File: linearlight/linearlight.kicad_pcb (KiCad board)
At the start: 2 copper layers, 136.7 x 59.7 mm, 72 parts, among them J1 Screw_Terminal, J2 Conn_01x04_Pin, J3 Conn_01x19_Socket, J4 Conn_01x19_Socket, J5 Conn_01x04_Pin, Q1 FQP30N06, Q2 FQP30N06, Q3 FQP30N06, Q4 FQP30N06, Q5 2N3904, Q6 2N3904, Q7 2N3904, Q8 2N3904, U1 TLV5620CN, U2 ESP32 DevKitC, U3 MC33204, U4 LM4040LP-2.5

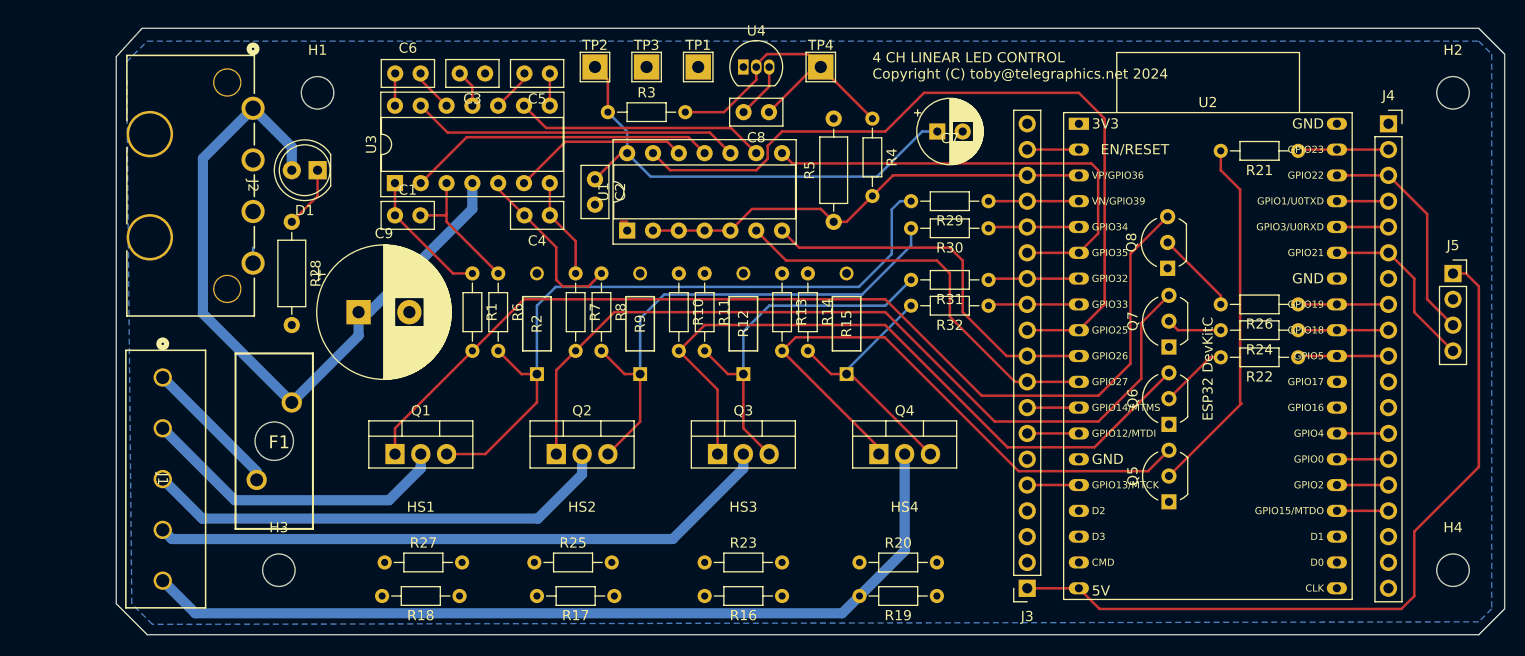
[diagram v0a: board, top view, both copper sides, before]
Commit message: Updates including 2nd DAC for nonlinear response.
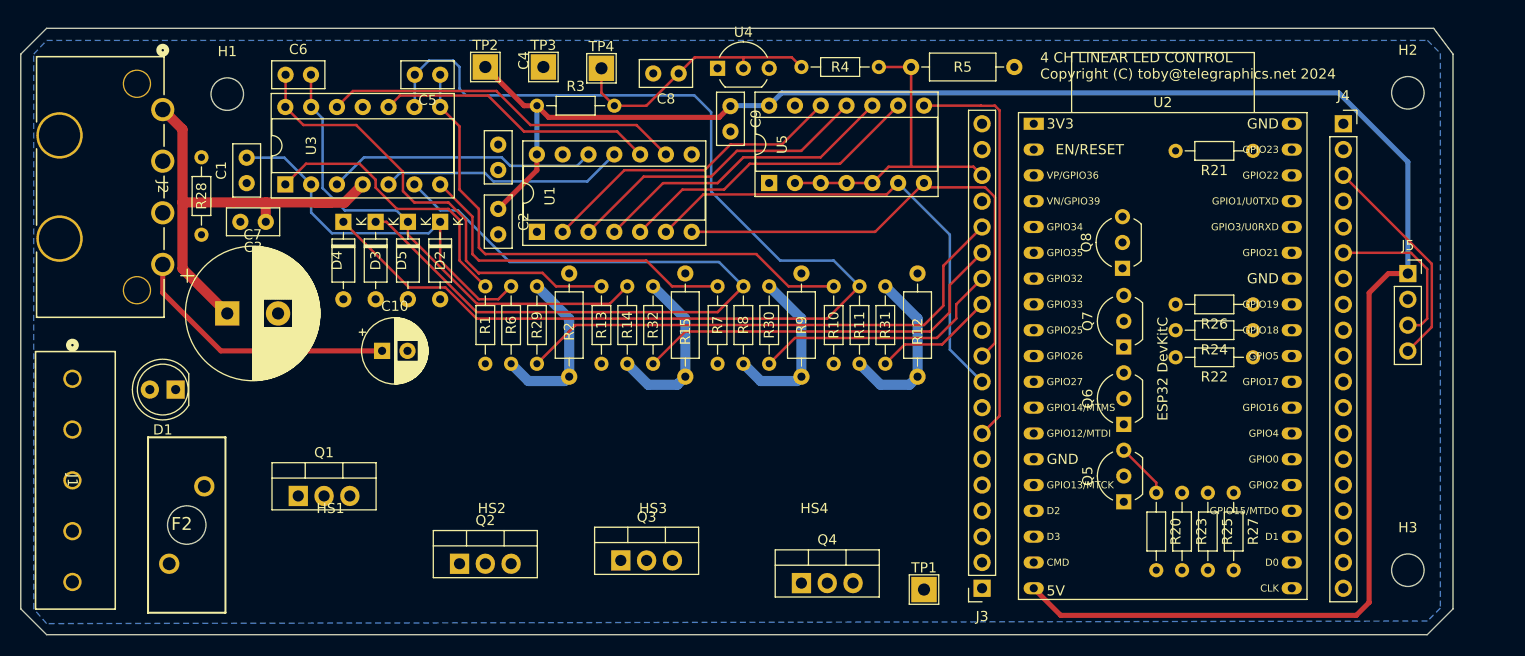
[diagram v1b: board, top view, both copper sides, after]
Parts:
- removed F1: Fuse, Fuse:01530008
- removed H4: MountingHole, MountingHole:MountingHole_3.2mm_M3
- removed R16, R17, R18, R19: 100k, Resistor_THT:R_Axial_DIN0204_L3.6mm_D1.6mm_P7.62mm_Horizontal
- added C10: 100u, Capacitor_THT:CP_Radial_D6.3mm_P2.50mm, F.Cu at (161.3, 116.8)
- added D2: 1N4148, Diode_THT:D_DO-35_SOD27_P7.62mm_Horizontal, F.Cu at (167.0, 104.1)
- added D3: 1N4148, Diode_THT:D_DO-35_SOD27_P7.62mm_Horizontal, F.Cu at (160.7, 104.1)
- added D4: 1N4148, Diode_THT:D_DO-35_SOD27_P7.62mm_Horizontal, F.Cu at (157.5, 104.1)
- added D5: 1N4148, Diode_THT:D_DO-35_SOD27_P7.62mm_Horizontal, F.Cu at (163.8, 104.1)
- added F2: Fuse, Fuse:01530008, F.Cu at (142.1, 134.0)
- added U5: TLV5620CN, Package_DIP:DIP-14_W7.62mm_Socket, F.Cu at (199.4, 100.3)
- C7: value 100u -> 2200uF; footprint Capacitor_THT:CP_Radial_D6.3mm_P2.50mm -> Capacitor_THT:CP_Radial_D13.0mm_P5.00mm
- C9: value 2200uF -> 1u; footprint Capacitor_THT:CP_Radial_D13.0mm_P5.00mm -> Capacitor_THT:C_Disc_D5.0mm_W2.5mm_P2.50mm
- H1, H2, H3: value MountingHole -> ~
- HS1, HS2, HS3, HS4: value Heatsink -> ~
- R12, R15, R2, R9: footprint Resistor_THT:RES_WLAR100FET -> Resistor_THT:R_Axial_DIN0207_L6.3mm_D2.5mm_P10.16mm_Horizontal
- R28: footprint Resistor_THT:R_Axial_DIN0207_L6.3mm_D2.5mm_P10.16mm_Horizontal -> Resistor_THT:R_Axial_DIN0204_L3.6mm_D1.6mm_P7.62mm_Horizontal
- R4: value 4.7k -> 10k
- U4: footprint Package_TO_SOT_THT:TO-92_Inline -> Package_TO_SOT_THT:TO-92_Inline_Wide
- moved H3 111.1 mm to (262.3, 138.4)
- moved R27 83.8 mm to (245.1, 130.8), turned to -90 degrees
- moved C7 72.1 mm to (146.1, 113.2)
- moved R25 66.6 mm to (242.6, 130.8), turned to -90 degrees
- moved TP1 56.0 mm to (214.6, 140.3)
- moved R23 47.5 mm to (240.0, 130.8), turned to -90 degrees
- moved R29 47.2 mm to (176.5, 118.1), turned to 90 degrees
- moved C9 41.8 mm to (195.6, 92.8), turned to -90 degrees
- moved R32 33.5 mm to (188.0, 118.1), turned to 90 degrees
- moved R20 30.0 mm to (237.5, 130.8), turned to -90 degrees
- moved C3 26.1 mm to (149.8, 104.1)
- moved D1 25.7 mm to (141.0, 120.7)
- moved R30 25.4 mm to (199.4, 118.1), turned to 90 degrees
- moved TP4 21.6 mm to (182.9, 89.0)
- moved R13 17.8 mm to (182.9, 110.5)
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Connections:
- C1 pad 2: Net-(U3A-IN+) -> Net-(D2-K)
- C4 pad 2: Net-(U3B-IN+) -> Net-(D3-K)
- C5 pad 2: Net-(U3C-IN+) -> Net-(D4-K)
- C6 pad 2: Net-(U3D-IN+) -> Net-(D5-K)
- C7 pad 1: +5V -> +12V
- C9 pad 1: +12V -> +5V
- J5 pad 3: Net-(J4-Pin_3) -> Net-(J4-Pin_6)
- J5 pad 4: Net-(J4-Pin_6) -> Net-(J4-Pin_3)
- R11 pad 1: Net-(U3C-IN+) -> Net-(D4-K)
- R14 pad 1: Net-(U3D-IN+) -> Net-(D5-K)
- R29 pad 1: Net-(J3-Pin_16) -> Net-(J3-Pin_15)
- R30 pad 1: Net-(J3-Pin_15) -> Net-(J3-Pin_13)
- R31 pad 1: Net-(J3-Pin_13) -> Net-(J3-Pin_12)
- R32 pad 1: Net-(J3-Pin_12) -> Net-(J3-Pin_14)
- R6 pad 1: Net-(U3A-IN+) -> Net-(D2-K)
- R8 pad 1: Net-(U3B-IN+) -> Net-(D3-K)
- U1 pad 2: Net-(J3-Pin_17) -> Net-(U1-REFA)
- U1 pad 3: Net-(J3-Pin_17) -> Net-(U1-REFB)
- U1 pad 4: Net-(J3-Pin_17) -> Net-(U1-REFC)
- U1 pad 5: Net-(J3-Pin_17) -> Net-(U1-REFD)
- U3 pad 10: Net-(U3C-IN+) -> Net-(U1-DACC)
- U3 pad 12: Net-(U3D-IN+) -> Net-(U1-DACD)
- U3 pad 13: Net-(U1-DACC) -> Net-(D5-K)
- U3 pad 2: Net-(U1-DACB) -> Net-(D2-K)
- U3 pad 3: Net-(U3A-IN+) -> Net-(U1-DACA)
- U3 pad 5: Net-(U3B-IN+) -> Net-(U1-DACB)
- U3 pad 6: Net-(U1-DACA) -> Net-(D3-K)
- U3 pad 9: Net-(U1-DACD) -> Net-(D4-K)
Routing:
- net Net-(D4-K): track 0.00 -> 118.6 mm
- net Net-(Q1-G): track 101.4 -> 0.00 mm
- net +5V: track 124.5 -> 215.9 mm
- net Net-(J1-Pin_5): track 86.4 -> 0.00 mm
- net Net-(Q2-G): track 83.7 -> 0.00 mm
- net Net-(D3-K): track 0.00 -> 77.5 mm
- net Net-(J3-Pin_11): track 77.1 -> 0.00 mm
- net Net-(Q3-G): track 69.1 -> 0.00 mm
- net Net-(J1-Pin_4): track 61.8 -> 0.00 mm
- net Net-(Q4-G): track 59.0 -> 5.51 mm
- net Net-(Q1-S): track 68.9 -> 16.8 mm
- net Net-(U3C-OUT): track 3.18 -> 55.1 mm
- net Net-(D5-K): track 0.00 -> 47.8 mm
- net Net-(J1-Pin_3): track 46.7 -> 0.00 mm
- net Net-(J3-Pin_15): track 8.89 -> 51.7 mm
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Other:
- board size 136.7 x 59.7 mm -> 141 x 59.7 mm

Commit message: PCB layout passes DRC.
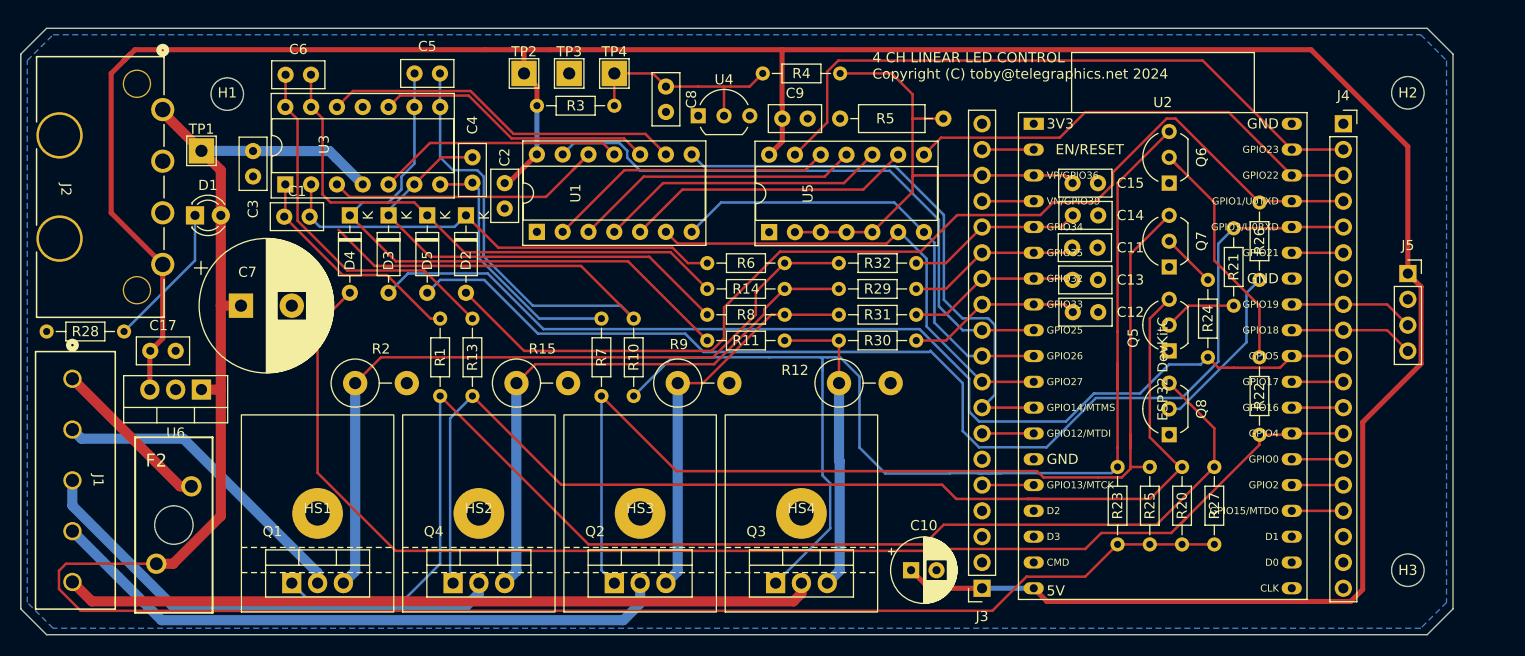
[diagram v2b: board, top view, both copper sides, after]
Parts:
- added C11: 0.1u, Capacitor_THT:C_Disc_D5.0mm_W2.5mm_P2.50mm, F.Cu at (231.7, 106.7)
- added C12: 0.1u, Capacitor_THT:C_Disc_D5.0mm_W2.5mm_P2.50mm, F.Cu at (231.8, 113.0)
- added C13: 0.1u, Capacitor_THT:C_Disc_D5.0mm_W2.5mm_P2.50mm, F.Cu at (231.8, 109.9)
- added C14: 0.1u, Capacitor_THT:C_Disc_D5.0mm_W2.5mm_P2.50mm, F.Cu at (231.8, 103.5)
- added C15: 0.1u, Capacitor_THT:C_Disc_D5.0mm_W2.5mm_P2.50mm, F.Cu at (231.8, 100.3)
- added C17: .1u, Capacitor_THT:C_Disc_D5.0mm_W2.5mm_P2.50mm, F.Cu at (138.5, 116.8)
- added U6: L7805, Package_TO_SOT_THT:TO-220-3_Vertical, F.Cu at (143.5, 120.7)
- D1: footprint LED_THT:LED_D5.0mm -> LED_THT:LED_D3.0mm
- HS1, HS2, HS3, HS4: footprint Heatsink:Max48 heatsink -> Heatsink:Max47 heatsink
- R12, R15, R2, R9: value 0.15 -> 0.5; footprint Resistor_THT:R_Axial_DIN0207_L6.3mm_D2.5mm_P10.16mm_Horizontal -> Resistor_THT:R_Axial_DIN0414_L11.9mm_D4.5mm_P5.08mm_Vertical
- R4: value 10k -> 2.2k
- moved TP1 83.2 mm to (143.5, 97.2)
- moved C10 56.4 mm to (213.4, 138.4)
- moved R29 38.1 mm to (213.9, 110.7), turned to 180 degrees
- moved Q4 34.3 mm to (168.3, 139.7)
- moved R32 27.7 mm to (213.9, 108.2), turned to 180 degrees
- moved Q6 24.2 mm to (238.8, 100.3)
- moved R2 21.1 mm to (158.6, 120.0), turned to 0 degrees
- moved R10 19.9 mm to (186.1, 113.7)
- moved R6 19.4 mm to (193.3, 108.2), turned to 0 degrees
- moved D1 17.3 mm to (142.9, 103.5), turned to 0 degrees
- moved Q8 17.0 mm to (238.8, 125.1)
- moved R15 16.6 mm to (174.5, 120.0), turned to 0 degrees
- moved R11 15.9 mm to (193.3, 115.8), turned to 0 degrees
- moved Q5 15.5 mm to (238.8, 116.8)
- moved Q3 15.4 mm to (200.0, 139.7)
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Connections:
- J4 pad 10: Net-(J4-Pin_10) -> Net-(D3-A)
- J4 pad 13: Net-(D2-A) -> Net-(D4-A)
- J4 pad 14: Net-(D3-A) -> Net-(J4-Pin_14)
- J4 pad 15: Net-(D4-A) -> Net-(J4-Pin_15)
- J4 pad 16: Net-(D5-A) -> Net-(J4-Pin_16)
- J4 pad 4: Net-(J4-Pin_4) -> Net-(D2-A)
- J4 pad 5: Net-(J4-Pin_5) -> Net-(D5-A)
- J5 pad 3: Net-(J4-Pin_6) -> Net-(J4-Pin_8)
- J5 pad 4: Net-(J4-Pin_3) -> Net-(J4-Pin_9)
- Q2 pad 2: Net-(J1-Pin_3) -> Net-(J1-Pin_4)
- Q3 pad 2: Net-(J1-Pin_4) -> Net-(J1-Pin_5)
- Q4 pad 2: Net-(J1-Pin_5) -> Net-(J1-Pin_3)
- R21 pad 1: Net-(J4-Pin_2) -> Net-(D5-A)
- R22 pad 1: Net-(J4-Pin_10) -> Net-(D4-A)
- R24 pad 1: Net-(J4-Pin_9) -> Net-(D3-A)
- R26 pad 1: Net-(J4-Pin_8) -> Net-(D2-A)
- R29 pad 1: Net-(J3-Pin_15) -> Net-(J3-Pin_14)
- R29 pad 2: Net-(Q1-S) -> Net-(Q4-S)
- R30 pad 1: Net-(J3-Pin_13) -> Net-(J3-Pin_12)
- R30 pad 2: Net-(Q2-S) -> Net-(Q3-S)
- R31 pad 1: Net-(J3-Pin_12) -> Net-(J3-Pin_13)
- R31 pad 2: Net-(Q3-S) -> Net-(Q2-S)
- R32 pad 1: Net-(J3-Pin_14) -> Net-(J3-Pin_15)
- R32 pad 2: Net-(Q4-S) -> Net-(Q1-S)
- U2 pad 23: Net-(D5-A) -> Net-(J4-Pin_16)
- U2 pad 24: Net-(D4-A) -> Net-(J4-Pin_15)
- U2 pad 25: Net-(D3-A) -> Net-(J4-Pin_14)
- U2 pad 26: Net-(D2-A) -> Net-(D4-A)
- U2 pad 29: Net-(J4-Pin_10) -> Net-(D3-A)
- U2 pad 34: Net-(J4-Pin_5) -> Net-(D5-A)
- U2 pad 35: Net-(J4-Pin_4) -> Net-(D2-A)
- U5 pad 13: unconnected-(U5-LDAC-Pad13) -> Net-(J4-Pin_2)
- U5 pad 8: Net-(J3-Pin_7) -> Net-(J4-Pin_3)
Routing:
- net +12V: track 44.6 -> 200.8 mm
- net Net-(D4-A): track 0.00 -> 129.6 mm
- net Net-(Q1-G): track 0.00 -> 128.6 mm
- net Net-(Q3-G): track 0.00 -> 125.3 mm
- net Net-(D5-A): track 0.00 -> 116.3 mm
- net Net-(Q4-G): track 5.51 -> 114.7 mm
- net Net-(D3-A): track 0.00 -> 106.2 mm
- net Net-(Q2-G): track 0.00 -> 104.4 mm
- net Net-(D2-A): track 0.00 -> 104.2 mm
- net Net-(J1-Pin_5): track 0.00 -> 73.9 mm
- net +5V: track 215.9 -> 286.3 mm
- net Net-(J4-Pin_2): track 0.00 -> 64.4 mm
- net Net-(J1-Pin_4): track 0.00 -> 62.2 mm
- net Net-(D4-K): track 118.6 -> 58.4 mm
- net Net-(J3-Pin_11): track 0.00 -> 59.9 mm
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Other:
- outline, holes or cut-outs redrawn

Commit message: Release candidate 1
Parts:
- added TP_VDAC1: VDAC, TestPoint:TestPoint_THTPad_2.5x2.5mm_Drill1.2mm, F.Cu at (216.4, 90.4)
- moved J5 2.05 mm to (262.1, 107.2)
- renumbered TP1 to TP+12, TP4 to TP+2.5, TP2 to TP+5, TP3 to TP_GND1
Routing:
- net Net-(J3-Pin_17): track 50.0 -> 56.7 mm
- net Net-(J4-Pin_8): track 12.3 -> 11.3 mm
- net Net-(J4-Pin_9): track 12.3 -> 11.3 mm
- net +5V: track 286.3 -> 287.3 mm
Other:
- board text added: "+ G R B W"
- board text added: "4 CHANNEL LINEAR LED CONTROL Copyright (C) toby@telegraphics.net 2024"
- board text added: "emilite 1.0"
- board text removed: "4 CH LINEAR LED CONTROL Copyright (C) toby@telegraphics.net 2024"

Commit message: Release candidate 2
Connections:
- U1 pad 13: Net-(J3-Pin_11) -> Net-(J3-Pin_10)
- U1 pad 6: Net-(J3-Pin_9) -> Net-(J3-Pin_8)
- U1 pad 7: Net-(J3-Pin_10) -> Net-(J3-Pin_9)
- U1 pad 8: Net-(J3-Pin_8) -> Net-(J3-Pin_11)
- U5 pad 6: Net-(J3-Pin_9) -> Net-(J3-Pin_8)
- U5 pad 7: Net-(J3-Pin_10) -> Net-(J3-Pin_9)
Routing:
- net Net-(Q3-G): track 125.3 -> 102.4 mm, vias 0 -> 1
- net Net-(J3-Pin_10): track 45.7 -> 60.7 mm
- net Net-(J3-Pin_11): track 59.9 -> 45.3 mm
- net Net-(J3-Pin_8): track 55.4 -> 49.8 mm
- net Net-(D5-A): track 116.3 -> 114.4 mm
- net Net-(D3-A): track 106.2 -> 104.3 mm
- net Net-(J3-Pin_9): track 47.1 -> 46.0 mm

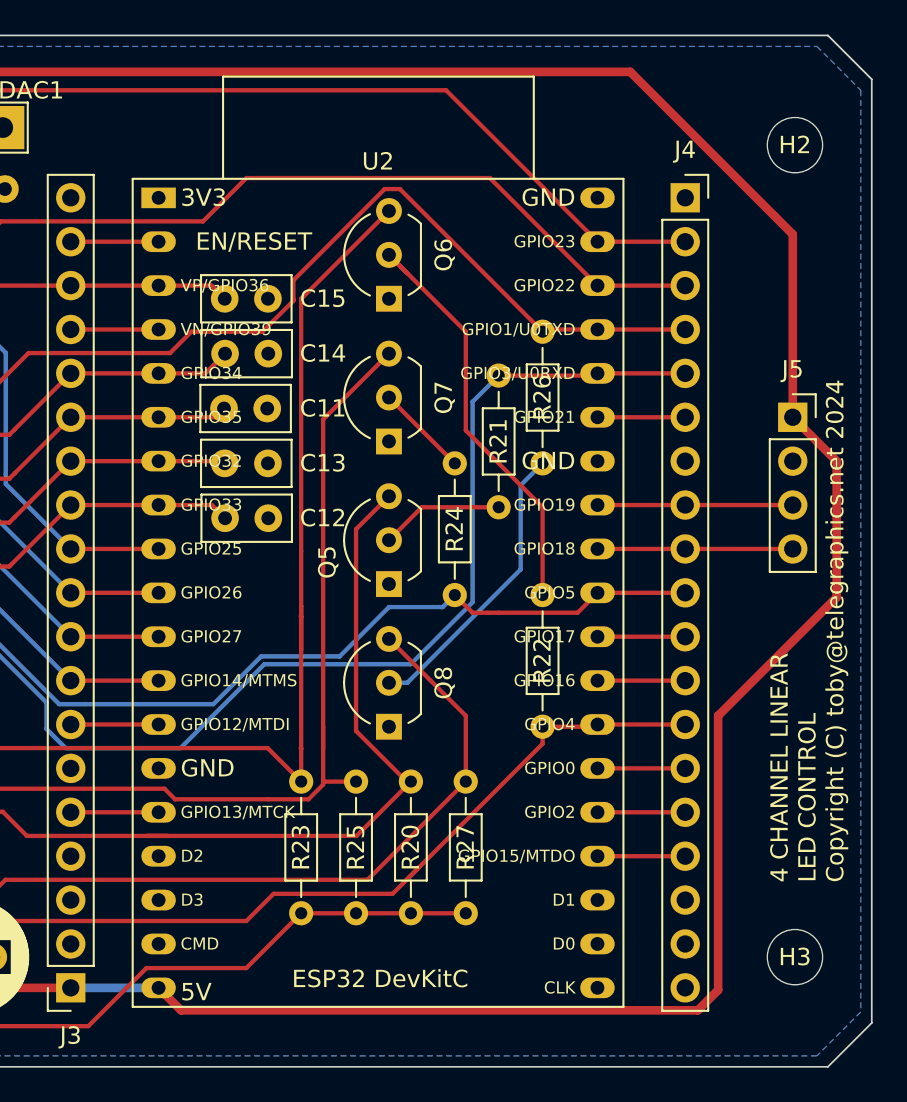
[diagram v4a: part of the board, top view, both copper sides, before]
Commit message: Add cnx for spectrometer.
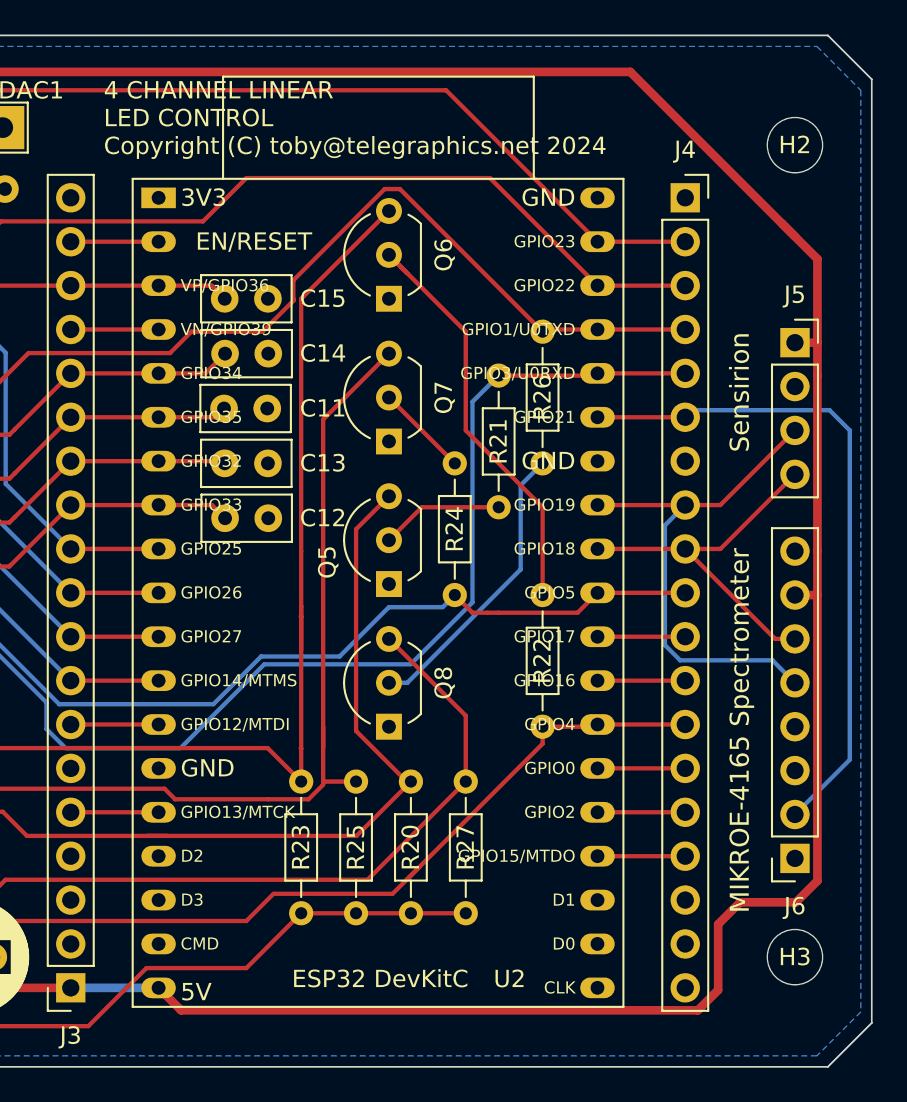
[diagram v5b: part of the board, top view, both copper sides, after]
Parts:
- added J6: Conn_01x08_Socket, Connector_PinSocket_2.54mm:PinSocket_1x08_P2.54mm_Vertical, F.Cu at (262.3, 132.7)
- moved J5 4.32 mm to (262.3, 102.9)
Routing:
- net Net-(J4-Pin_6): track 5.08 -> 38.8 mm
- net Net-(J4-Pin_8): track 11.3 -> 30.2 mm
- net Net-(J4-Pin_9): track 11.3 -> 21.7 mm
- net +5V: track 287.3 -> 291.9 mm
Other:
- board text added: "MIKROE-4165 Spectrometer"
- board text added: "Sensirion"

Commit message: Release candidate 3
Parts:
- moved R22 27.3 mm to (247.7, 97.8), turned to 180 degrees
- moved J5 21.0 mm to (261.6, 123.8)
- moved R26 20.3 mm to (247.7, 122.6), turned to 180 degrees
- moved J6 15.3 mm to (261.6, 117.5)
- moved R24 12.5 mm to (247.7, 106.0), turned to 180 degrees
- moved R21 9.86 mm to (247.7, 114.3), turned to 180 degrees
- moved Q5 2.18 mm to (236.6, 116.8)
- moved Q6 2.18 mm to (236.6, 100.3)
- moved Q7 2.18 mm to (236.6, 108.6)
- moved Q8 2.18 mm to (236.6, 125.1)
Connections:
- J4 pad 11: Net-(J4-Pin_11) -> Net-(D5-A)
- J4 pad 12: Net-(J4-Pin_12) -> Net-(D2-A)
- J4 pad 13: Net-(D4-A) -> Net-(J4-Pin_13)
- J4 pad 4: Net-(D2-A) -> Net-(J4-Pin_4)
- J4 pad 5: Net-(D5-A) -> Net-(J4-Pin_5)
- J4 pad 8: Net-(J4-Pin_8) -> Net-(D4-A)
- J5 pad 3: Net-(J4-Pin_8) -> Net-(J4-Pin_13)
- J5 pad 4: Net-(J4-Pin_9) -> Net-(J4-Pin_6)
- J6 pad 2: Net-(J4-Pin_6) -> Net-(J4-Pin_9)
- J6 pad 5: Net-(J4-Pin_8) -> Net-(J4-Pin_13)
- J6 pad 6: Net-(J4-Pin_9) -> Net-(J4-Pin_6)
- U2 pad 26: Net-(D4-A) -> Net-(J4-Pin_13)
- U2 pad 27: Net-(J4-Pin_12) -> Net-(D2-A)
- U2 pad 28: Net-(J4-Pin_11) -> Net-(D5-A)
- U2 pad 31: Net-(J4-Pin_8) -> Net-(D4-A)
- U2 pad 34: Net-(D5-A) -> Net-(J4-Pin_5)
- U2 pad 35: Net-(D2-A) -> Net-(J4-Pin_4)
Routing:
- net Net-(D4-A): track 129.6 -> 167.7 mm, vias 0 -> 1
- net Net-(J4-Pin_13): track 0.00 -> 32.0 mm
- net Net-(J4-Pin_8): track 30.2 -> 0.00 mm
- net Net-(Q3-G): track 102.4 -> 129.5 mm, vias 1 -> 0
- net Net-(Q6-B): track 24.4 -> 3.45 mm
- net Net-(D3-A): track 104.3 -> 123.0 mm
- net Net-(Q8-B): track 17.0 -> 3.45 mm
- net Net-(J4-Pin_9): track 21.7 -> 11.0 mm
- net +5V: track 291.9 -> 299.1 mm
- net Net-(J4-Pin_5): track 0.00 -> 5.44 mm
- net Net-(J4-Pin_4): track 0.00 -> 5.08 mm
- net Net-(J4-Pin_12): track 5.08 -> 0.00 mm
- net Net-(J4-Pin_11): track 5.08 -> 0.00 mm
- net Net-(D5-A): track 114.4 -> 109.4 mm
- net Net-(Q5-B): track 7.14 -> 3.45 mm
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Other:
- board text added: "“The light that burns twice as bright, burns half as long.”"

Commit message: Production 2024-02-18
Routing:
- net Net-(U3C-OUT): track 71.3 -> 38.5 mm
- net Net-(D4-A): track 167.7 -> 158.3 mm
- net +5V: track 299.1 -> 292.9 mm
- net Net-(Q3-G): track 129.5 -> 126.9 mm
- net Net-(U1-DACA): track 29.2 -> 27.0 mm
- net Net-(J3-Pin_10): track 60.7 -> 59.9 mm
- net Net-(Q4-G): track 114.5 -> 113.9 mm
- net Net-(Q2-G): track 103.5 -> 102.9 mm
- net Net-(D3-K): track 46.8 -> 46.3 mm
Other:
- board text added: "13V max"
- board text added: "5V"
